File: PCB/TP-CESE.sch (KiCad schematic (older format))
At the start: 38 parts, among them J1 Screw_Terminal_01x04, J3 Screw_Terminal_01x02, J4 Conn_01x04_Male, J5 test, Q1 IRF540N, Q2 IRF540N, Q3 IRF540N, Q4 IRF540N, U1 4N25, U2 4N25, U3 4N25, U4 4N25, U5 ADS1015IDGS

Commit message: Correcciones Charlie , agrego hojas de datos
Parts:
- D1, D2, D3: footprint Diode_THT:D_5W_P10.16mm_Horizontal -> Diode_SMD:D_SOD-123
- D4: value (1n4148)x4 -> D; footprint Diode_THT:D_5W_P10.16mm_Horizontal -> Diode_SMD:D_SOD-123
- Q1, Q2, Q3, Q4: footprint Package_TO_SOT_THT:TO-262-3_Vertical -> Package_TO_SOT_SMD:TO-263-2
- R1, R2, R3, R4: value 100 -> 180; footprint Resistor_SMD:R_2010_5025Metric_Pad1.52x2.65mm_HandSolder -> Resistor_SMD:R_1210_3225Metric
- R10, R11, R12, R5, R6, R7, R8, R9: footprint Resistor_SMD:R_2512_6332Metric_Pad1.52x3.35mm_HandSolder -> Resistor_SMD:R_1210_3225Metric
- U1, U2, U3, U4: footprint Package_DIP:DIP-6_W7.62mm -> Package_DIP:SMDIP-6_W9.53mm
- renumbered XA-2 to X1, XA-1 to X1
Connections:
- net GND: now also J3.1 (Pin_1); no longer J3.2 (Pin_2)
- net VCC: now also J3.2 (Pin_2); no longer J3.1 (Pin_1)
- net at D1.2 (A), Q1.2 (D): now also J1.4 (Pin_4); no longer J1.1 (Pin_1)
- net at D2.2 (A), Q2.2 (D): now also J1.3 (Pin_3); no longer J1.2 (Pin_2)
- net at D3.2 (A), Q3.2 (D): now also J1.2 (Pin_2); no longer J1.3 (Pin_3)
- net at D4.2 (A), Q4.2 (D): now also J1.1 (Pin_1); no longer J1.4 (Pin_4)
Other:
- note added: "Conversor Addc 12 bits \n"
- note added: "D:1N4148\n"
- note added: "Diodos Flyback\n"
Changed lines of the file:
@@
 encoding utf-8
 Sheet 1 1
-Title "Sebastian Herrera- DCI-CESE-FIUBA"
-Date "2020-09-12"
+Title "TP-Driver Motor PaP-DCI-CESE-FIUBA"
+Date "2020-10-08"
 Rev "1"
-Comp "Proyecto -TP "
+Comp "Sebastian Herrera"
 Comment1 ""
 Comment2 ""
@@
 F 0 "U1" H 4900 2225 50  0000 C CNN
 F 1 "4N25" H 4900 2134 50  0000 C CNN
-F 2 "Package_DIP:DIP-6_W7.62mm" H 4700 1700 50  0001 L CIN
+F 2 "Package_DIP:SMDIP-6_W9.53mm" H 4700 1700 50  0001 L CIN
 F 3 "https://www.vishay.com/docs/83725/4n25.pdf" H 4900 1900 50  0001 L CNN
 	1    4900 1900
@@
 F 0 "U2" H 4900 3125 50  0000 C CNN
 F 1 "4N25" H 4900 3034 50  0000 C CNN
-F 2 "Package_DIP:DIP-6_W7.62mm" H 4700 2600 50  0001 L CIN
+F 2 "Package_DIP:SMDIP-6_W9.53mm" H 4700 2600 50  0001 L CIN
 F 3 "https://www.vishay.com/docs/83725/4n25.pdf" H 4900 2800 50  0001 L CNN
 	1    4900 2800
@@
 F 0 "U3" H 4900 4025 50  0000 C CNN
 F 1 "4N25" H 4900 3934 50  0000 C CNN
-F 2 "Package_DIP:DIP-6_W7.62mm" H 4700 3500 50  0001 L CIN
+F 2 "Package_DIP:SMDIP-6_W9.53mm" H 4700 3500 50  0001 L CIN
 F 3 "https://www.vishay.com/docs/83725/4n25.pdf" H 4900 3700 50  0001 L CNN
 	1    4900 3700
@@
 F 0 "U4" H 4900 4875 50  0000 C CNN
 F 1 "4N25" H 4900 4784 50  0000 C CNN
-F 2 "Package_DIP:DIP-6_W7.62mm" H 4700 4350 50  0001 L CIN
+F 2 "Package_DIP:SMDIP-6_W9.53mm" H 4700 4350 50  0001 L CIN
 F 3 "https://www.vishay.com/docs/83725/4n25.pdf" H 4900 4550 50  0001 L CNN
 	1    4900 4550
@@
 P 4250 2150
 F 0 "R1" H 4320 2196 50  0000 L CNN
-F 1 "100" H 4320 2105 50  0000 L CNN
-F 2 "Resistor_SMD:R_2010_5025Metric_Pad1.52x2.65mm_HandSolder" V 4180 2150 50  0001 C CNN
+F 1 "180" H 4320 2105 50  0000 L CNN
+F 2 "Resistor_SMD:R_1210_3225Metric" V 4180 2150 50  0001 C CNN
 F 3 "~" H 4250 2150 50  0001 C CNN
 	1    4250 2150
@@
 P 4250 3050
 F 0 "R2" H 4320 3096 50  0000 L CNN
-F 1 "100" H 4320 3005 50  0000 L CNN
-F 2 "Resistor_SMD:R_2010_5025Metric_Pad1.52x2.65mm_HandSolder" V 4180 3050 50  0001 C CNN
+F 1 "180" H 4320 3005 50  0000 L CNN
+F 2 "Resistor_SMD:R_1210_3225Metric" V 4180 3050 50  0001 C CNN
 F 3 "~" H 4250 3050 50  0001 C CNN
 	1    4250 3050
@@
 P 4250 3950
 F 0 "R3" H 4320 3996 50  0000 L CNN
-F 1 "100" H 4320 3905 50  0000 L CNN
-F 2 "Resistor_SMD:R_2010_5025Metric_Pad1.52x2.65mm_HandSolder" V 4180 3950 50  0001 C CNN
+F 1 "180" H 4320 3905 50  0000 L CNN
+F 2 "Resistor_SMD:R_1210_3225Metric" V 4180 3950 50  0001 C CNN
 F 3 "~" H 4250 3950 50  0001 C CNN
 	1    4250 3950
@@
 P 4250 4800
 F 0 "R4" H 4320 4846 50  0000 L CNN
-F 1 "100" H 4320 4755 50  0000 L CNN
-F 2 "Resistor_SMD:R_2010_5025Metric_Pad1.52x2.65mm_HandSolder" V 4180 4800 50  0001 C CNN
+F 1 "180" H 4320 4755 50  0000 L CNN
+F 2 "Resistor_SMD:R_1210_3225Metric" V 4180 4800 50  0001 C CNN
 F 3 "~" H 4250 4800 50  0001 C CNN
 	1    4250 4800
@@
 F 0 "R5" H 5470 1796 50  0000 L CNN
 F 1 "100" H 5470 1705 50  0000 L CNN
-F 2 "Resistor_SMD:R_2512_6332Metric_Pad1.52x3.35mm_HandSolder" V 5330 1750 50  0001 C CNN
+F 2 "Resistor_SMD:R_1210_3225Metric" V 5330 1750 50  0001 C CNN
 F 3 "~" H 5400 1750 50  0001 C CNN
 	1    5400 1750
@@
 F 0 "R6" H 5470 2696 50  0000 L CNN
 F 1 "100" H 5470 2605 50  0000 L CNN
-F 2 "Resistor_SMD:R_2512_6332Metric_Pad1.52x3.35mm_HandSolder" V 5330 2650 50  0001 C CNN
+F 2 "Resistor_SMD:R_1210_3225Metric" V 5330 2650 50  0001 C CNN
 F 3 "~" H 5400 2650 50  0001 C CNN
 	1    5400 2650
@@
 F 0 "R7" H 5470 3596 50  0000 L CNN
 F 1 "100" H 5470 3505 50  0000 L CNN
-F 2 "Resistor_SMD:R_2512_6332Metric_Pad1.52x3.35mm_HandSolder" V 5330 3550 50  0001 C CNN
+F 2 "Resistor_SMD:R_1210_3225Metric" V 5330 3550 50  0001 C CNN
 F 3 "~" H 5400 3550 50  0001 C CNN
 	1    5400 3550
@@
 F 0 "R8" H 5470 4446 50  0000 L CNN
 F 1 "100" H 5470 4355 50  0000 L CNN
-F 2 "Resistor_SMD:R_2512_6332Metric_Pad1.52x3.35mm_HandSolder" V 5330 4400 50  0001 C CNN
+F 2 "Resistor_SMD:R_1210_3225Metric" V 5330 4400 50  0001 C CNN
 F 3 "~" H 5400 4400 50  0001 C CNN
 	1    5400 4400
@@
 F 0 "R9" V 5300 1900 50  0000 C CNN
 F 1 "1K" V 5400 1900 50  0000 C CNN
-F 2 "Resistor_SMD:R_2512_6332Metric_Pad1.52x3.35mm_HandSolder" V 5430 2000 50  0001 C CNN
+F 2 "Resistor_SMD:R_1210_3225Metric" V 5430 2000 50  0001 C CNN
 F 3 "~" H 5500 2000 50  0001 C CNN
 	1    5500 2000
@@
 F 0 "R10" V 5700 2800 50  0000 C CNN
 F 1 "1K" V 5600 2800 50  0000 C CNN
-F 2 "Resistor_SMD:R_2512_6332Metric_Pad1.52x3.35mm_HandSolder" V 5430 2900 50  0001 C CNN
+F 2 "Resistor_SMD:R_1210_3225Metric" V 5430 2900 50  0001 C CNN
 F 3 "~" H 5500 2900 50  0001 C CNN
 	1    5500 2900
@@
 F 0 "R11" V 5300 3700 50  0000 C CNN
 F 1 "1K" V 5400 3700 50  0000 C CNN
-F 2 "Resistor_SMD:R_2512_6332Metric_Pad1.52x3.35mm_HandSolder" V 5430 3800 50  0001 C CNN
+F 2 "Resistor_SMD:R_1210_3225Metric" V 5430 3800 50  0001 C CNN
 F 3 "~" H 5500 3800 50  0001 C CNN
 	1    5500 3800
@@
 F 0 "R12" V 5300 4550 50  0000 C CNN
 F 1 "1K" V 5400 4550 50  0000 C CNN
-F 2 "Resistor_SMD:R_2512_6332Metric_Pad1.52x3.35mm_HandSolder" V 5430 4650 50  0001 C CNN
+F 2 "Resistor_SMD:R_1210_3225Metric" V 5430 4650 50  0001 C CNN
 F 3 "~" H 5500 4650 50  0001 C CNN
 	1    5500 4650
@@
 F 0 "Q1" H 6404 1746 50  0000 L CNN
 F 1 "IRF540N" H 6404 1655 50  0000 L CNN
-F 2 "Package_TO_SOT_THT:TO-262-3_Vertical" H 6450 1625 50  0001 L CIN
+F 2 "Package_TO_SOT_SMD:TO-263-2" H 6450 1625 50  0001 L CIN
 F 3 "http://www.irf.com/product-info/datasheets/data/irf540n.pdf" H 6200 1700 50  0001 L CNN
 	1    6200 1700
@@
 F 0 "Q2" H 6404 2646 50  0000 L CNN
 F 1 "IRF540N" H 6404 2555 50  0000 L CNN
-F 2 "Package_TO_SOT_THT:TO-262-3_Vertical" H 6450 2525 50  0001 L CIN
+F 2 "Package_TO_SOT_SMD:TO-263-2" H 6450 2525 50  0001 L CIN
 F 3 "http://www.irf.com/product-info/datasheets/data/irf540n.pdf" H 6200 2600 50  0001 L CNN
 	1    6200 2600
@@
 F 0 "Q3" H 6404 3496 50  0000 L CNN
 F 1 "IRF540N" H 6404 3405 50  0000 L CNN
-F 2 "Package_TO_SOT_THT:TO-262-3_Vertical" H 6450 3375 50  0001 L CIN
+F 2 "Package_TO_SOT_SMD:TO-263-2" H 6450 3375 50  0001 L CIN
 F 3 "http://www.irf.com/product-info/datasheets/data/irf540n.pdf" H 6200 3450 50  0001 L CNN
 	1    6200 3450
@@
 F 0 "Q4" H 6404 4346 50  0000 L CNN
 F 1 "IRF540N" H 6404 4255 50  0000 L CNN
-F 2 "Package_TO_SOT_THT:TO-262-3_Vertical" H 6450 4225 50  0001 L CIN
+F 2 "Package_TO_SOT_SMD:TO-263-2" H 6450 4225 50  0001 L CIN
 F 3 "http://www.irf.com/product-info/datasheets/data/irf540n.pdf" H 6200 4300 50  0001 L CNN
 	1    6200 4300
@@
 Text Notes 7800 3600 0    50   ~ 0
 Conector a bobinas \nMotor paso a paso\n
-Text Notes 2400 3550 0    50   ~ 0
+Text Notes 2450 3500 0    50   ~ 0
 conector a edu-ciaa\n1->GPIO1\n2->GPIO2\n3->GPIO3\n4->GPIO4
 $Comp
@@
 L Connector:Screw_Terminal_01x04 J1
 U 1 1 5F65097C
-P 8500 3100
-F 0 "J1" H 8580 3092 50  0000 L CNN
-F 1 "Screw_Terminal_01x04" H 8580 3001 50  0000 L CNN
-F 2 "TerminalBlock_Phoenix:TerminalBlock_Phoenix_MKDS-1,5-4-5.08_1x04_P5.08mm_Horizontal" H 8500 3100 50  0001 C CNN
-F 3 "~" H 8500 3100 50  0001 C CNN
-	1    8500 3100
-	1    0    0    -1
+P 8500 3200
+F 0 "J1" H 8580 3192 50  0000 L CNN
+F 1 "Screw_Terminal_01x04" H 8580 3101 50  0000 L CNN
+F 2 "TerminalBlock_Phoenix:TerminalBlock_Phoenix_MKDS-1,5-4-5.08_1x04_P5.08mm_Horizontal" H 8500 3200 50  0001 C CNN
+F 3 "~" H 8500 3200 50  0001 C CNN
+	1    8500 3200
+	1    0    0    1
 $EndComp
 $Comp
@@
 $EndComp
 Text Label 4150 1000 0    50   ~ 0
-VCC
+GND1
 Wire Wire Line
 	3850 1000 4150 1000
 Text Label 4150 1100 0    50   ~ 0
-GND1
+VCC
 Wire Wire Line
 	3850 1100 4150 1100
@@
 Alimentacion fuente de alimentacion\ndiferente de Edu-Ciaa \nTension de alimentacion: 5Volts /3 Amp\n
 $Comp
-L Poncho_Esqueleto:Conn_Poncho2P_2x_20x2 XA-2
-U 2 1 5F6D5FC5
-P 1550 1100
-F 0 "XA-2" H 1900 1647 60  0000 C CNN
-F 1 "Conn_Poncho2P_2x_20x2" H 1900 1541 60  0000 C CNN
-F 2 "Poncho_Esqueleto:Conn_Poncho_Chico" H 1550 1100 60  0001 C CNN
-F 3 "" H 1550 1100 60  0000 C CNN
-	2    1550 1100
-	1    0    0    -1
-$EndComp
-$Comp
-L Poncho_Esqueleto:Conn_Poncho2P_2x_20x2 XA-1
+L Poncho_Esqueleto:Conn_Poncho2P_2x_20x2 X1
 U 1 1 5F6D7DDE
 P 2200 5350
-F 0 "XA-1" H 2550 5897 60  0000 C CNN
+F 0 "X1" H 2550 5897 60  0000 C CNN
 F 1 "Conn_Poncho2P_2x_20x2" H 2550 5791 60  0000 C CNN
 F 2 "Poncho_Esqueleto:Conn_Poncho_Chico" H 2200 5350 60  0001 C CNN
@@
 F 0 "D1" V 7154 2780 50  0000 L CNN
 F 1 "D" V 7250 2800 50  0000 L CNN
-F 2 "Diode_THT:D_5W_P10.16mm_Horizontal" H 7200 2700 50  0001 C CNN
+F 2 "Diode_SMD:D_SOD-123" H 7200 2700 50  0001 C CNN
 F 3 "~" H 7200 2700 50  0001 C CNN
 	1    7200 2700
@@
 F 0 "D2" V 7404 2780 50  0000 L CNN
 F 1 "D" V 7495 2780 50  0000 L CNN
-F 2 "Diode_THT:D_5W_P10.16mm_Horizontal" H 7450 2700 50  0001 C CNN
+F 2 "Diode_SMD:D_SOD-123" H 7450 2700 50  0001 C CNN
 F 3 "~" H 7450 2700 50  0001 C CNN
 	1    7450 2700
@@
 F 0 "D3" V 7654 2780 50  0000 L CNN
 F 1 "D" V 7745 2780 50  0000 L CNN
-F 2 "Diode_THT:D_5W_P10.16mm_Horizontal" H 7700 2700 50  0001 C CNN
+F 2 "Diode_SMD:D_SOD-123" H 7700 2700 50  0001 C CNN
 F 3 "~" H 7700 2700 50  0001 C CNN
 	1    7700 2700
@@
 P 7950 2700
 F 0 "D4" V 7904 2780 50  0000 L CNN
-F 1 "(1n4148)x4" V 7995 2780 50  0000 L CNN
-F 2 "Diode_THT:D_5W_P10.16mm_Horizontal" H 7950 2700 50  0001 C CNN
+F 1 "D" V 7995 2780 50  0000 L CNN
+F 2 "Diode_SMD:D_SOD-123" H 7950 2700 50  0001 C CNN
 F 3 "~" H 7950 2700 50  0001 C CNN
 	1    7950 2700
@@
 Text Notes 5600 1350 0    50   ~ 0
 Alimentacion de 5 volts DC \n\n
+Text Notes 3050 7000 0    50   ~ 0
+Conversor Addc 12 bits \n
+Wire Notes Line
+	3650 6600 3450 6850
+Wire Notes Line
+	3450 6850 3300 6850
+$Comp
+L Poncho_Esqueleto:Conn_Poncho2P_2x_20x2 X1
+U 2 1 5F6D5FC5
+P 1550 1100
+F 0 "X1" H 1900 1647 60  0000 C CNN
+F 1 "Conn_Poncho2P_2x_20x2" H 1900 1541 60  0000 C CNN
+F 2 "Poncho_Esqueleto:Conn_Poncho_Chico" H 1550 1100 60  0001 C CNN
+F 3 "" H 1550 1100 60  0000 C CNN
+	2    1550 1100
+	1    0    0    -1
+$EndComp
+Text Notes 7000 2350 0    50   ~ 0
+Diodos Flyback\n
+Wire Notes Line
+	7050 2400 7150 2600
+Text Notes 8250 2700 0    50   ~ 0
+D:1N4148\n
 $EndSCHEMATC

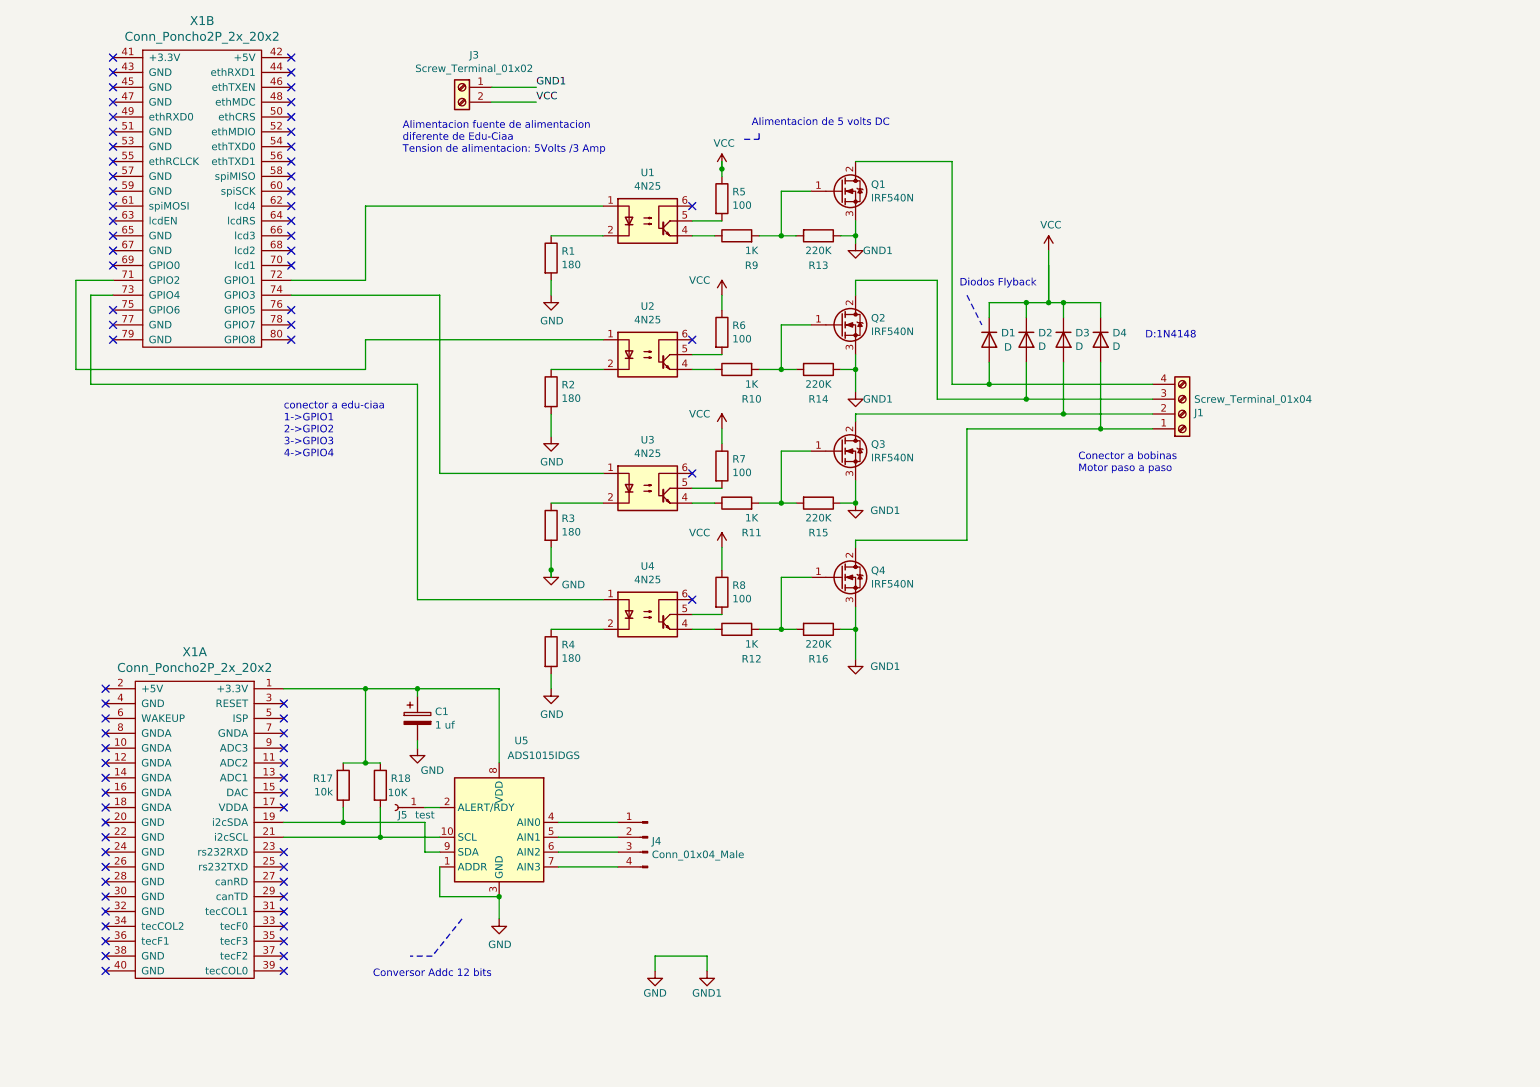
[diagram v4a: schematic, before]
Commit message: Correciones al esquematico, de acuerdo a sugerencia de Diego Brengi(Profesor)  y Carlos Carreño Romano(revisor)
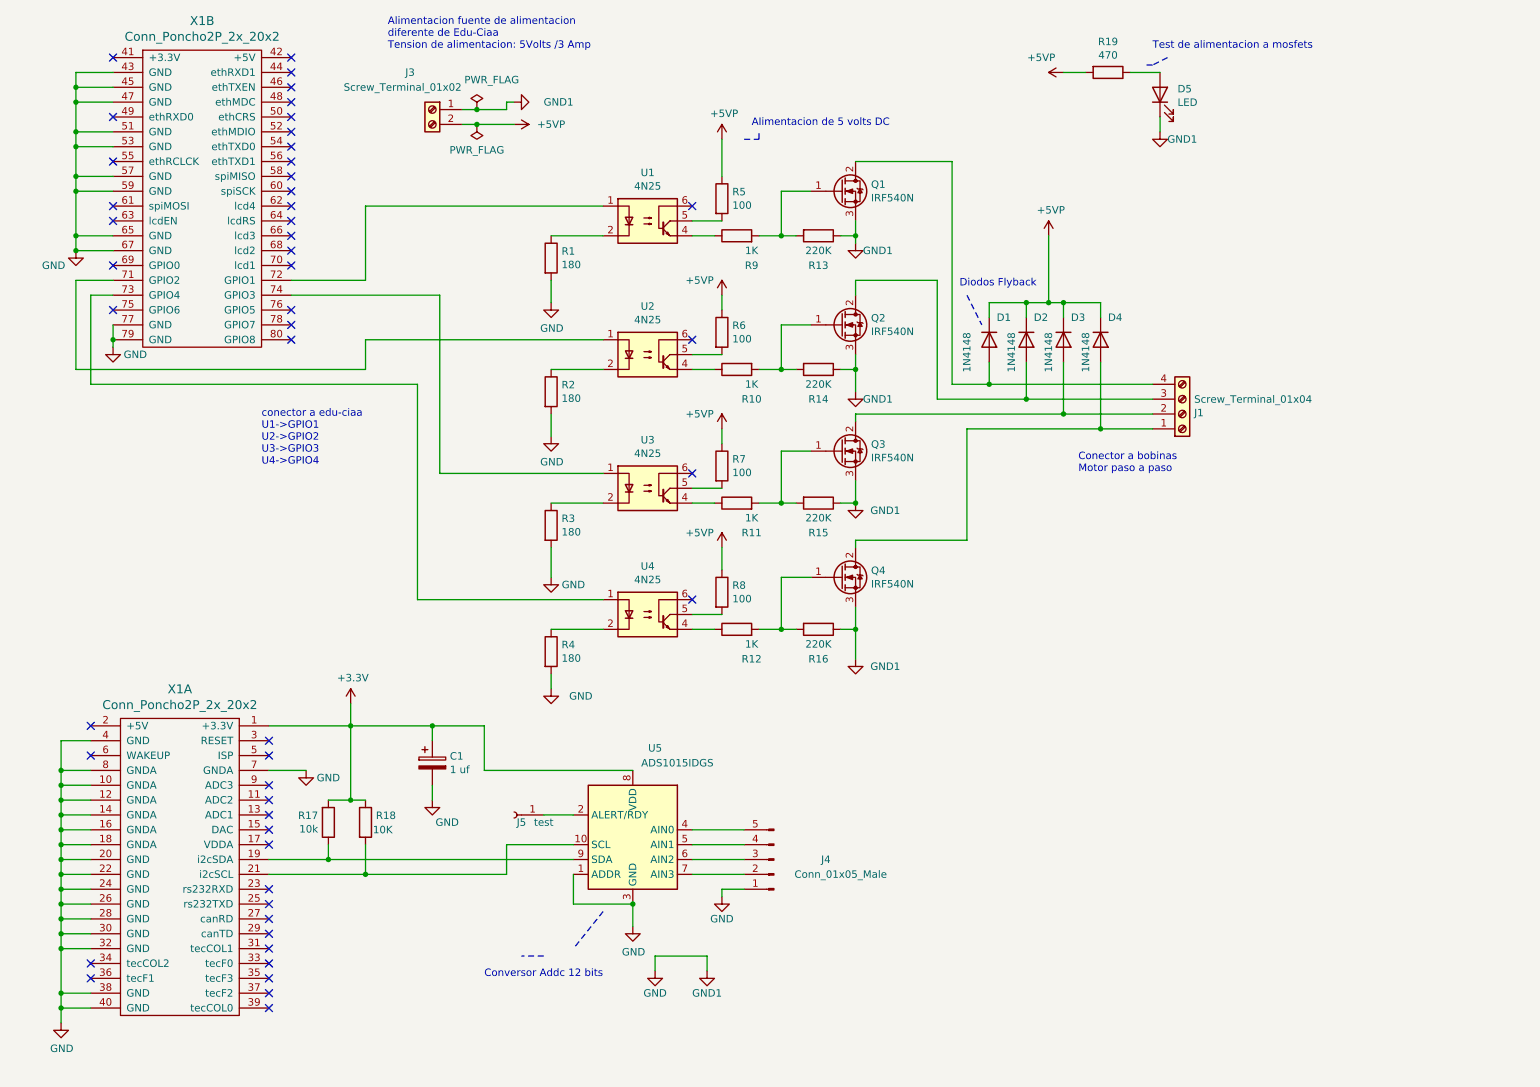
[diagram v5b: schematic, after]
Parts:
- removed J4: Conn_01x04_Male, Connector_PinHeader_2.00mm:PinHeader_1x04_P2.00mm_Vertical, symbol Connector:Conn_01x04_Male
- added D5: LED, LED_SMD:LED_0805_2012Metric_Pad1.15x1.40mm_HandSolder, symbol Device:LED
- added J4: Conn_01x05_Male, Connector_PinHeader_2.00mm:PinHeader_1x05_P2.00mm_Vertical, symbol Connector:Conn_01x05_Male
- added R19: 470, Resistor_SMD:R_0805_2012Metric_Pad1.20x1.40mm_HandSolder, symbol Device:R
- C1: footprint Capacitor_SMD:CP_Elec_4x5.4 -> Connector_PinHeader_2.00mm:PinHeader_1x05_P2.00mm_Vertical
- D1, D2, D3: value D -> 1N4148; footprint Diode_SMD:D_SOD-123 -> Diode_SMD:D_SC-80_HandSoldering; Digikey# (none) -> 1N4148FS-ND
- D4: value D -> 1N4148; footprint Diode_SMD:D_SOD-123 -> Diode_SMD:D_SC-80_HandSoldering; digikey# (none) -> 1N4148FS-ND
- Q1: footprint Package_TO_SOT_SMD:TO-263-2 -> Package_TO_SOT_THT:TO-262-3_Vertical; digikey# (none) -> IRF540NLPBF-ND
- Q2, Q3, Q4: footprint Package_TO_SOT_SMD:TO-263-2 -> Package_TO_SOT_THT:TO-262-3_Vertical; Digikey# (none) -> IRF540NLPBF-ND
- R1, R10, R11, R12, R13, R14, R15, R16, R17, R18, R2, R3, R4, R5, R6, R7, R8, R9: footprint Resistor_SMD:R_1210_3225Metric -> Resistor_SMD:R_0805_2012Metric_Pad1.20x1.40mm_HandSolder
- U1, U2, U3, U4: footprint Package_DIP:SMDIP-6_W9.53mm -> Package_DIP:DIP-6_W7.62mm; Digikey# (none) -> 4N25VS-ND
- U5: Digikey# (none) -> 296-41185-1-ND
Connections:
- net GND: now also X1.10 (GNDA), X1.12 (GNDA), X1.14 (GNDA), X1.16 (GNDA), X1.18 (GNDA), X1.20 (GND), X1.22 (GND), X1.24 (GND), X1.26 (GND), X1.28 (GND), X1.30 (GND), X1.32 (GND), X1.38 (GND), X1.4 (GND), X1.40 (GND), X1.43 (GND), X1.45 (GND), X1.47 (GND), X1.51 (GND), X1.53 (GND), X1.57 (GND), X1.59 (GND), X1.65 (GND), X1.67 (GND), X1.7 (GNDA), X1.77 (GND), X1.79 (GND), X1.8 (GNDA), D5.1 (K), J4.1 (Pin_1)
- net +3V3: now reaches C1.1, R17.2, R18.1, U5.8 (VDD), X1.1 (+3.3V)
- net at U5.4 (AIN0): now also J4.5 (Pin_5)
- net at U5.5 (AIN1): now also J4.4 (Pin_4)
- net at U5.6 (AIN2): now also J4.3 (Pin_3)
- net at U5.7 (AIN3): now also J4.2 (Pin_2)
- net VCC renamed +5VP
- net +5VP: now also R19.2
- new net: D5.2 (A), R19.1
- no-connect marks 77 -> 49
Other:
- note added: "Test de alimentacion a mosfets"
- note added: "conector a edu-ciaa\nU1->GPIO1\nU2->GPIO2\nU3->GPIO3\nU4->GPIO4"
- note removed: "D:1N4148\n"
- note removed: "conector a edu-ciaa\n1->GPIO1\n2->GPIO2\n3->GPIO3\n4->GPIO4"
- moved on the sheet: C1, J3, J5, R17, R18, U5, X1A

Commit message: Posicionamiento de componenetes en PCB
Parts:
- C1: footprint Connector_PinHeader_2.00mm:PinHeader_1x05_P2.00mm_Vertical -> Capacitor_SMD:CP_Elec_4x4.5
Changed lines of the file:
@@
 F 0 "C1" H 3568 5596 50  0000 L CNN
 F 1 "1 uf" H 3568 5505 50  0000 L CNN
-F 2 "Connector_PinHeader_2.00mm:PinHeader_1x05_P2.00mm_Vertical" H 3488 5400 50  0001 C CNN
+F 2 "Capacitor_SMD:CP_Elec_4x4.5" H 3488 5400 50  0001 C CNN
 F 3 "~" H 3450 5550 50  0001 C CNN
 	1    3450 5550
